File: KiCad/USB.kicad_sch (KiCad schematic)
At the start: 4 parts, among them U8 usb, U9 HT42B534-2

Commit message: footprint added
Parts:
- TP10: footprint (none) -> TestPoint:TestPoint_Loop_D2.54mm_Drill1.5mm_Beaded
- U8: footprint (none) -> footprint:MICRO-USB-SMD_MICROXNJ
- U9: footprint (none) -> footprint:SOIC-8_L4.9-W3.9-P1.27-LS6.0-BL; Extended Part Cost (none) -> 3; JLC code (none) -> C493294; Part name (none) -> HT42B534-2; cost per unit (none) -> 0.7554
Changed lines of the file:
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@@
       (effects (font (size 1.27 1.27)) (justify right))
     )
-    (property "Footprint" "" (at 205.74 146.05 0)
+    (property "Footprint" "TestPoint:TestPoint_Loop_D2.54mm_Drill1.5mm_Beaded" (at 205.74 146.05 0)
       (effects (font (size 1.27 1.27)) hide)
     )
@@
       (effects (font (size 1.27 1.27)) (justify left))
     )
-    (property "Footprint" "" (at 215.9 143.51 0)
+    (property "Footprint" "TestPoint:TestPoint_Loop_D2.54mm_Drill1.5mm_Beaded" (at 215.9 143.51 0)
       (effects (font (size 1.27 1.27)) hide)
     )
@@
       (effects (font (size 1.27 1.27)))
     )
-    (property "Footprint" "" (at 236.22 142.24 0)
+    (property "Footprint" "footprint:SOIC-8_L4.9-W3.9-P1.27-LS6.0-BL" (at 236.22 142.24 0)
       (effects (font (size 1.27 1.27)) hide)
     )
@@
       (effects (font (size 1.27 1.27)) hide)
     )
-    (property "Extended Part Cost" "" (at 236.22 142.24 0)
+    (property "Extended Part Cost" "3" (at 236.22 142.24 0)
       (effects (font (size 1.27 1.27)) hide)
     )
-    (property "JLC code" "" (at 236.22 142.24 0)
+    (property "JLC code" "C493294" (at 236.22 142.24 0)
       (effects (font (size 1.27 1.27)) hide)
     )
-    (property "Part name" "" (at 236.22 142.24 0)
+    (property "Part name" "HT42B534-2" (at 236.22 142.24 0)
       (effects (font (size 1.27 1.27)) hide)
     )
-    (property "cost per unit" "" (at 236.22 142.24 0)
+    (property "cost per unit" "0.7554" (at 236.22 142.24 0)
       (effects (font (size 1.27 1.27)) hide)
     )
@@
       (effects (font (size 1.27 1.27)))
     )
-    (property "Footprint" "" (at 191.77 148.59 0)
+    (property "Footprint" "footprint:MICRO-USB-SMD_MICROXNJ" (at 191.77 148.59 0)
       (effects (font (size 1.27 1.27)) hide)
     )

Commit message: gerber power changed
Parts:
- TP10: footprint TestPoint:TestPoint_Loop_D2.54mm_Drill1.5mm_Beaded -> footprint:Testpoint_2.54mm
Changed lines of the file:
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@@
       (effects (font (size 1.27 1.27)) (justify right))
     )
-    (property "Footprint" "TestPoint:TestPoint_Loop_D2.54mm_Drill1.5mm_Beaded" (at 205.74 146.05 0)
+    (property "Footprint" "footprint:Testpoint_2.54mm" (at 205.74 146.05 0)
       (effects (font (size 1.27 1.27)) hide)
     )
@@
       (effects (font (size 1.27 1.27)) (justify left))
     )
-    (property "Footprint" "TestPoint:TestPoint_Loop_D2.54mm_Drill1.5mm_Beaded" (at 215.9 143.51 0)
+    (property "Footprint" "footprint:Testpoint_2.54mm" (at 215.9 143.51 0)
       (effects (font (size 1.27 1.27)) hide)
     )

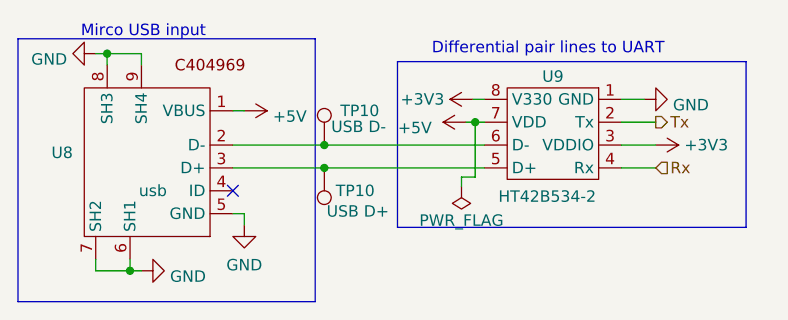
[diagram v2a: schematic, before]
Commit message: powwer 5v line seperation
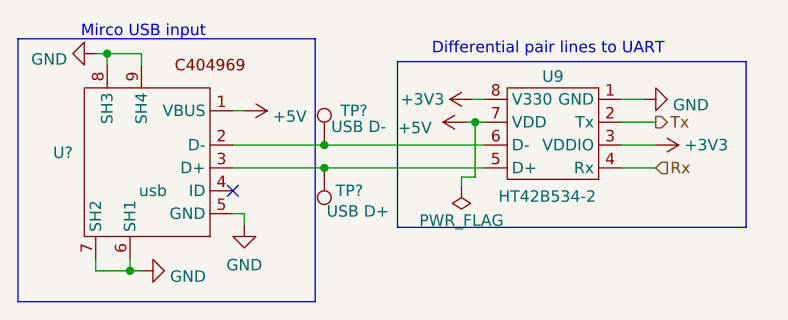
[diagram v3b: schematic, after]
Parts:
- renumbered TP10 to TP?, U8 to U?
